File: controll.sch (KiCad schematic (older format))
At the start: 0 parts

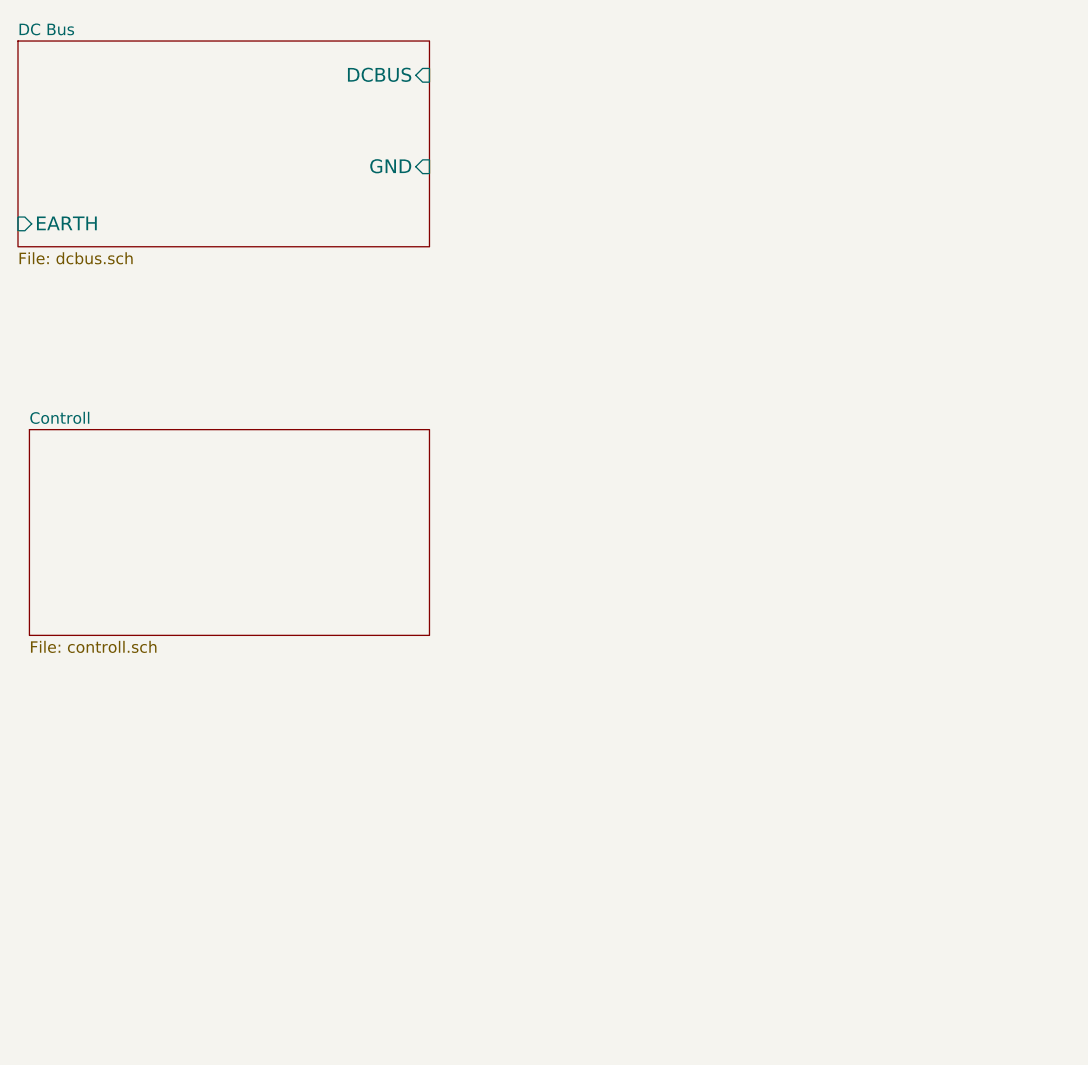
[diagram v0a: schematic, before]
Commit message: add placeholder for controll schematics
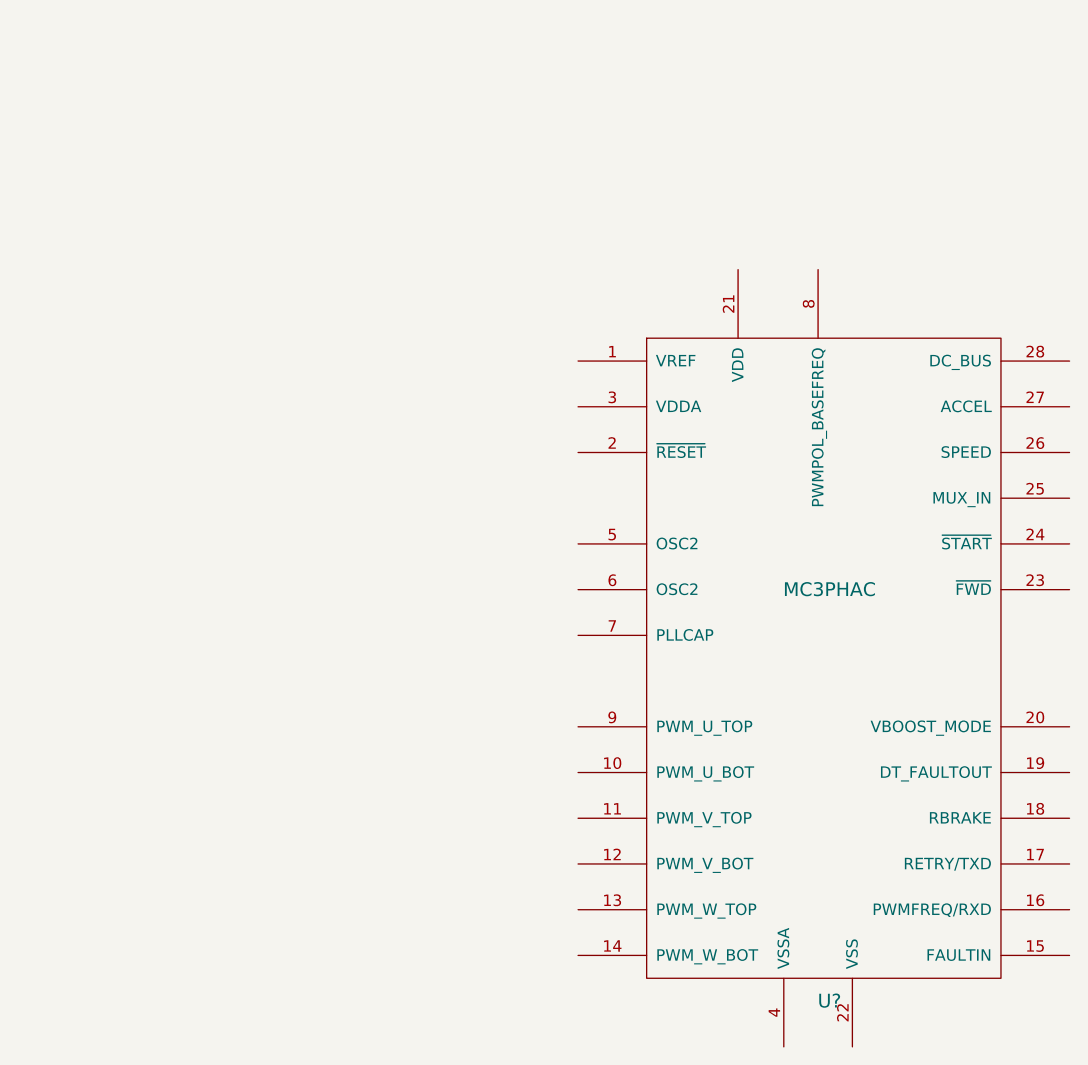
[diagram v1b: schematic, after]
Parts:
- added U?: MC3PHAC, symbol MC3PHAC
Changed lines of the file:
@@
 $Descr A4 11693 8268
 encoding utf-8
-Sheet 1 3
+Sheet 3 3
 Title ""
 Date ""
@@
 Comment4 ""
 $EndDescr
-$Sheet
-S 1450 1400 1800 900
-U 5377D90A
-F0 "DC Bus" 50
-F1 "dcbus.sch" 50
-F2 "DCBUS" I R 3250 1550 60
-F3 "GND" I R 3250 1950 60
-F4 "EARTH" I L 1450 2200 60
-$EndSheet
-$Sheet
-S 1500 3100 1750 900
-U 537BA57E
-F0 "Controll" 50
-F1 "controll.sch" 50
-$EndSheet
+$Comp
+L MC3PHAC U?
+U 1 1 537BA586
+P 4950 4000
+F 0 "U?" H 5000 2400 60  0000 C CNN
+F 1 "MC3PHAC" H 5000 4200 60  0000 C CNN
+F 2 "" H 5250 4450 60  0000 C CNN
+F 3 "" H 5250 4450 60  0000 C CNN
+	1    4950 4000
+	1    0    0    -1
+$EndComp
 $EndSCHEMATC

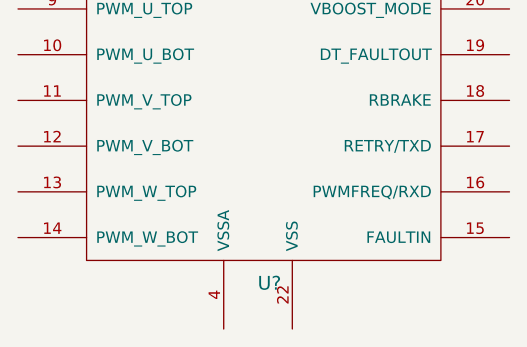
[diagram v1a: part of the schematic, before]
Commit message: add snubbing, mov for the main cap protection and a bleeder resistor for the main cap. add annotations finally
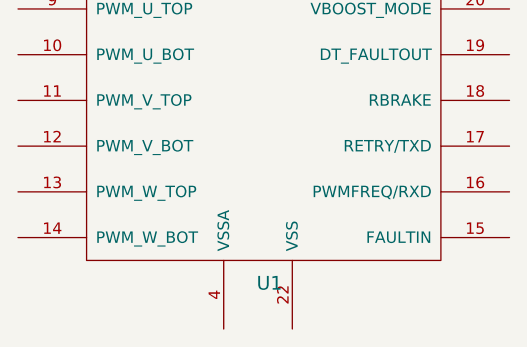
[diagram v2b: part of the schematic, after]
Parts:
- gave numbers to parts that had none: 1
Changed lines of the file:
@@
 $EndDescr
 $Comp
-L MC3PHAC U?
+L MC3PHAC U1
 U 1 1 537BA586
 P 4950 4000
-F 0 "U?" H 5000 2400 60  0000 C CNN
+F 0 "U1" H 5000 2400 60  0000 C CNN
 F 1 "MC3PHAC" H 5000 4200 60  0000 C CNN
 F 2 "" H 5250 4450 60  0000 C CNN

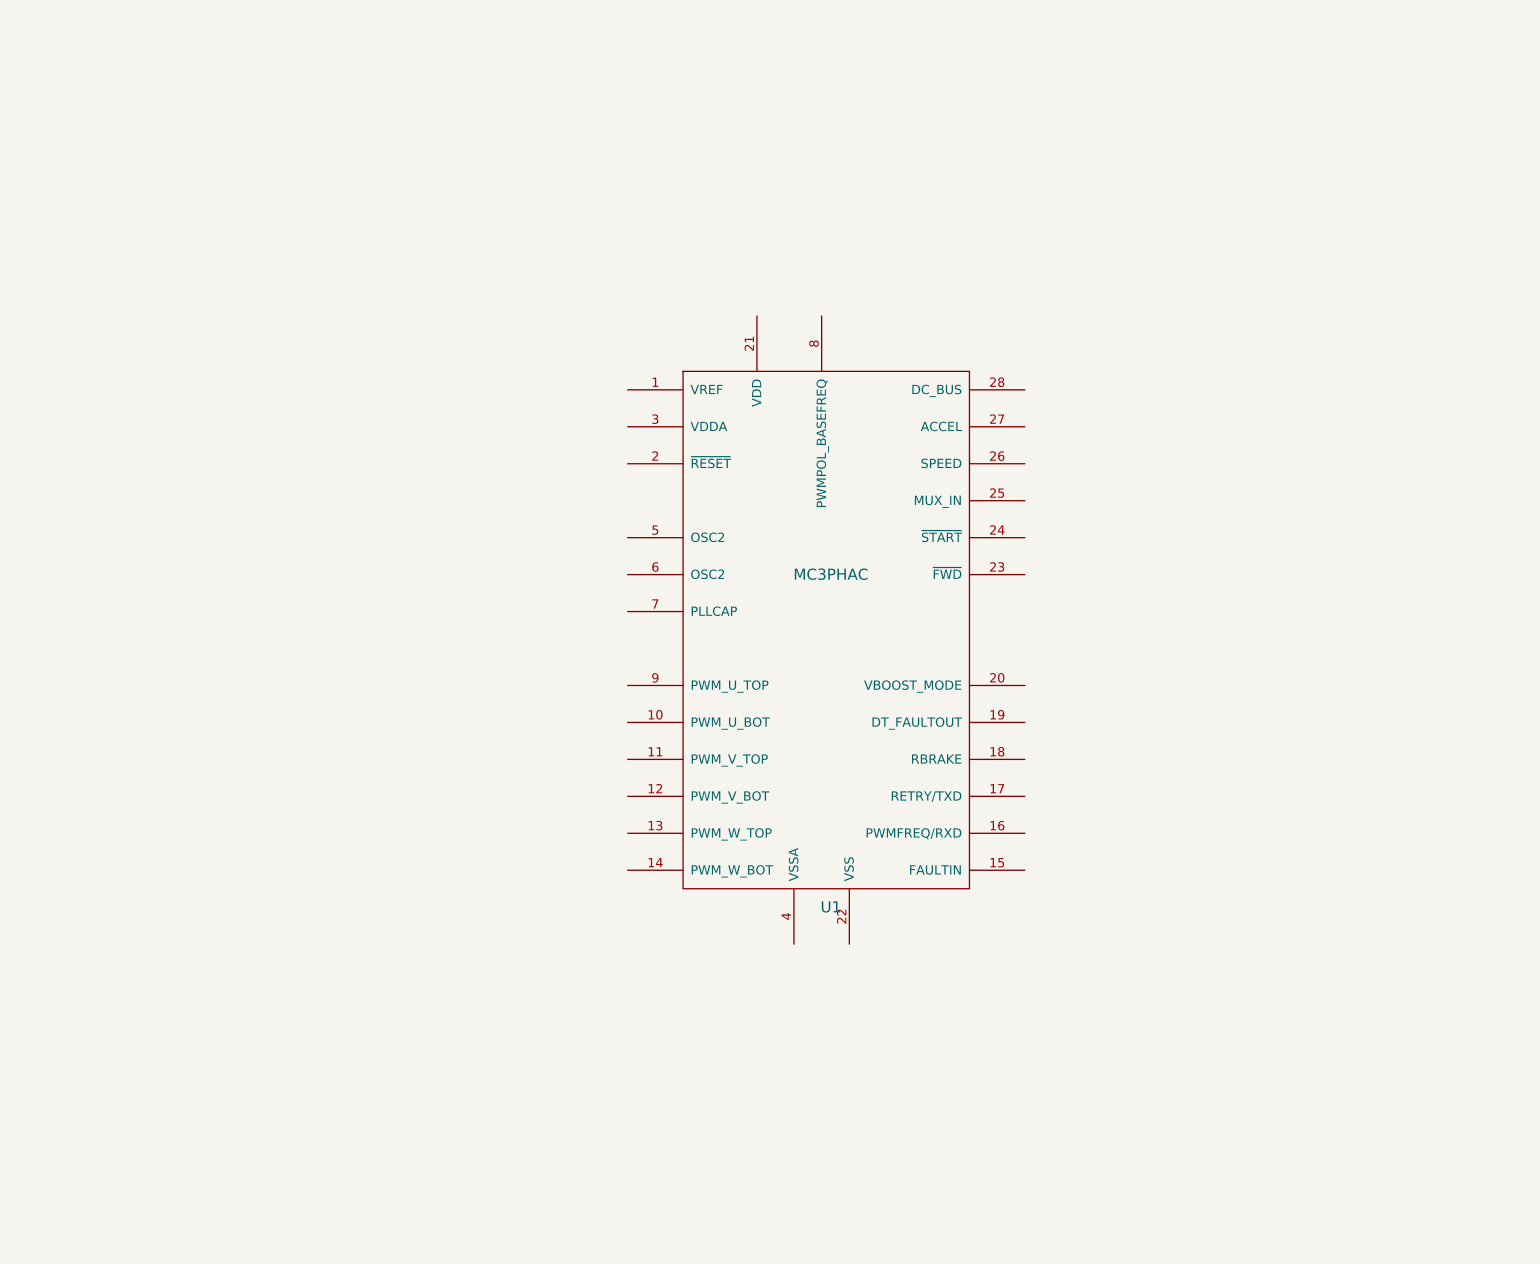
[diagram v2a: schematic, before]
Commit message: started populating contoll part
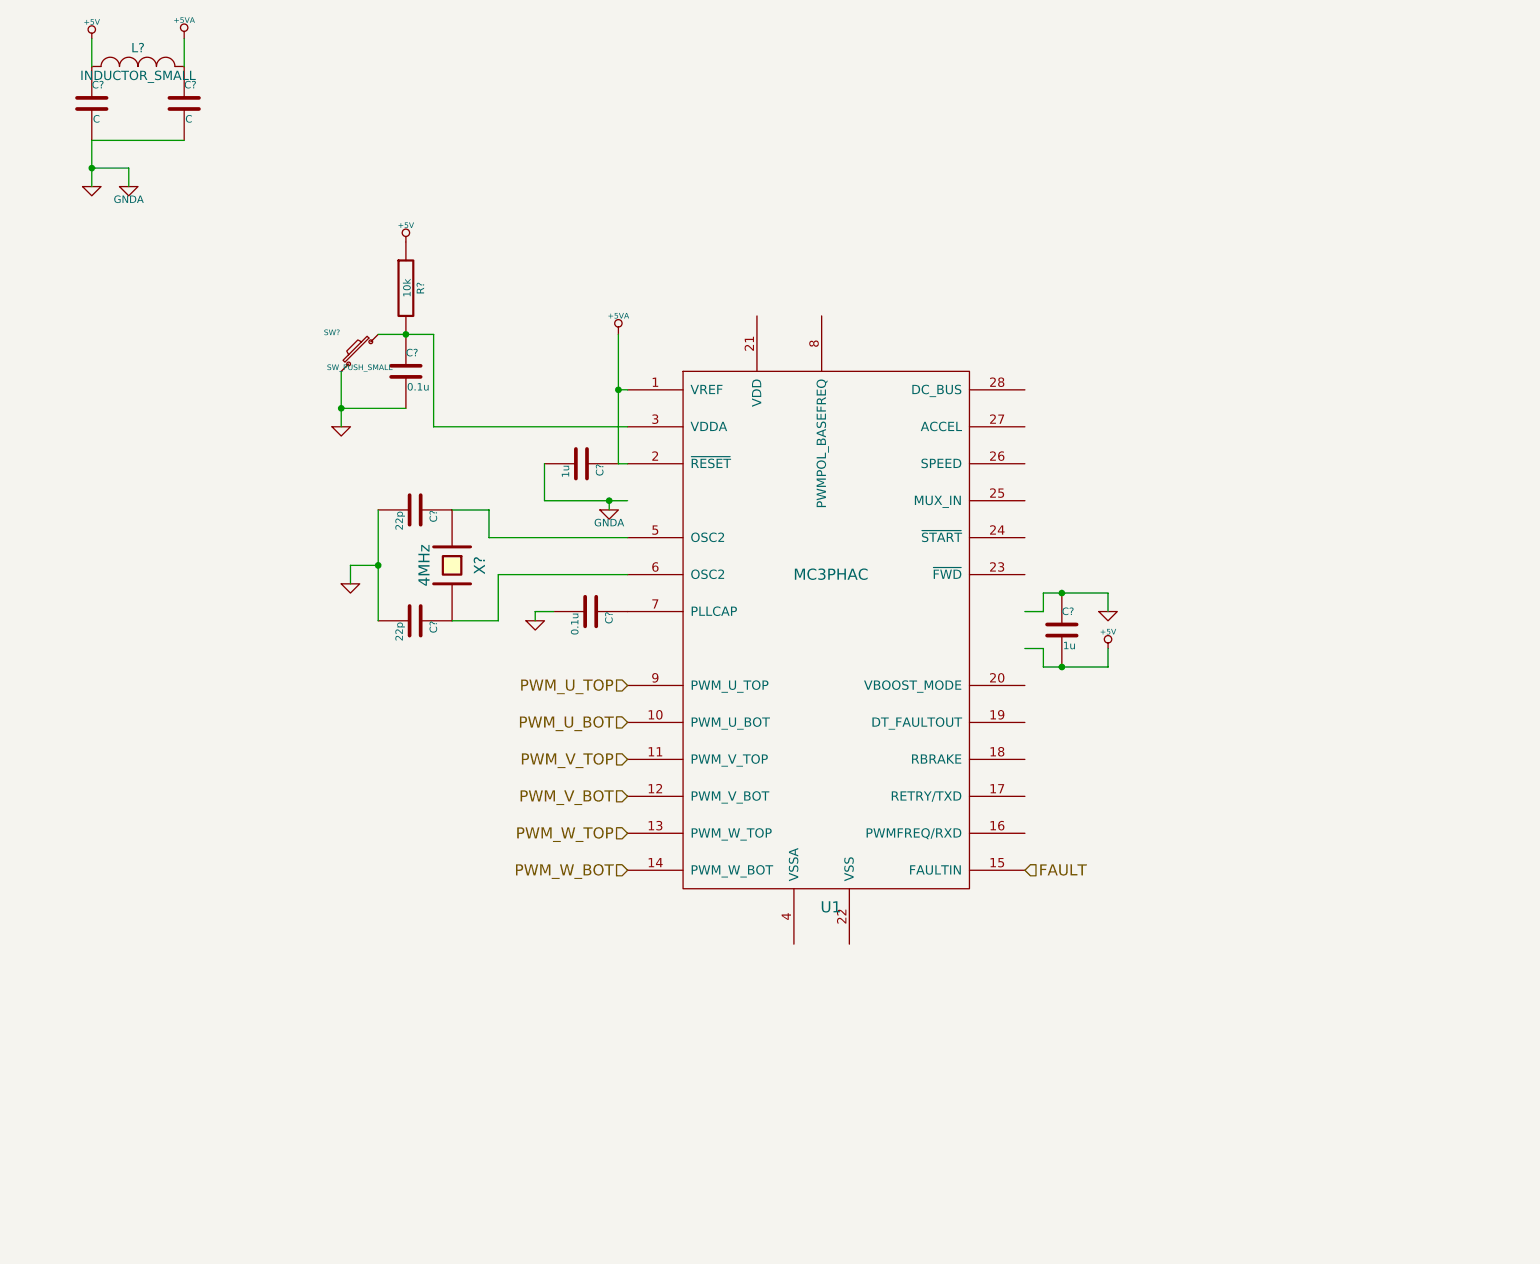
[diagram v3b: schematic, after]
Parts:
- added C? (x2): 22p, symbol C
- added C? (x2): 0.1u, symbol C
- added C? (x2): 1u, symbol C
- added C? (x2): C, symbol C
- added L?: INDUCTOR_SMALL, symbol INDUCTOR_SMALL
- added R?: 10k, symbol R
- added SW?: SW_PUSH_SMALL, symbol SW_PUSH_SMALL
- added X?: 4MHz, symbol CRYSTAL
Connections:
- net labels added: +5V, +5VA, FAULT, GND, GNDA, PWM_U_BOT, PWM_U_TOP, PWM_V_BOT, PWM_V_TOP, PWM_W_BOT, PWM_W_TOP
- wire segments 0 -> 36

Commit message: begin working on output power stage
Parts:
- removed SW?: SW_PUSH_SMALL, symbol SW_PUSH_SMALL
- added C14, C18: 100uF, symbol CP1
- added C15: 100nF, symbol C
- added C16: 10nF, symbol C
- added C17: 1nF, symbol C
- added JP1: 50Hz -, symbol JUMPER
- added JP2: 50Hz +, symbol JUMPER
- added JP3: 60Hz -, symbol JUMPER
- added JP4: 60Hz +, symbol JUMPER
- added P1: CONN_12, symbol CONN_12
- added P2, P3: CONN_6, symbol CONN_6
- added P4: CONN_4, symbol CONN_4
- added R10, R11, R12, R9: R, symbol R
- added R13, R14: 10k, symbol R
- added R6: 6.8k, symbol R
- added R7, R8: 4.7k, symbol R
- added SW1: SPST, symbol SPST
- C7: renamed from C?; value C -> 1uF
- gave numbers to parts that had none: 10
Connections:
- net labels added: ACCEL, DCBUSSENSE, RBRAKE, RXD, SPEED, TXD, ~FWD, ~START
- wire segments 36 -> 101
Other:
- moved on the sheet: C11, C13, C8, R5

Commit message: populating boards
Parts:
- added C?: 1n, symbol C
- added IC1: FOD8012, SOP-8, symbol FOD8012
- added R?: 100R, symbol R
- added R?: 4.7k, symbol R
- added SW4: PC/STANDALONE, symbol SWITCH_INV
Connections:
- net +5V: now also IC1.1, R?.1; no longer P4.4 (P4)
- net FAULT: now also C?.1, R?.1, R?.2; no longer U1.15 (FAULTIN)
- net GND: now also C?.2, IC1.4, SW4.3; no longer P4.2 (P2)
- net RXD: now also IC1.7; no longer R12.2, U1.16 (PWMFREQ/RXD)
- net TXD: now also IC1.6; no longer R11.2, U1.17 (RETRY/TXD)
- net at U1.20 (VBOOST_MODE): now also SW4.2; no longer R9.2
- new net: R?.2, U1.15 (FAULTIN)
- new net: IC1.2, R12.2, U1.16 (PWMFREQ/RXD)
- new net: IC1.3, R11.2, U1.17 (RETRY/TXD)
- new net: R9.2, SW4.1
- new net GND_UART: IC1.5, P4.2 (P2)
- new net V_UART: IC1.8, P4.4 (P4)
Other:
- moved on the sheet: R9

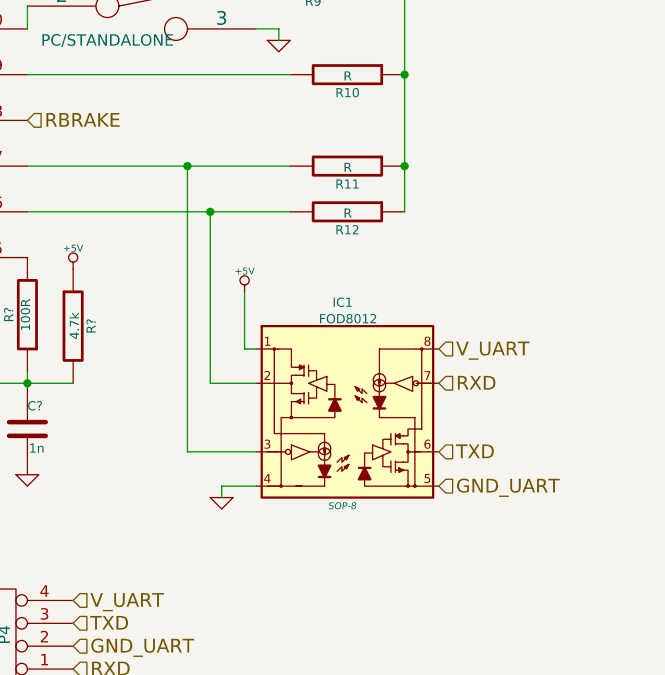
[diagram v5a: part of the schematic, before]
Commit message: fod8012 changed to cpc5001
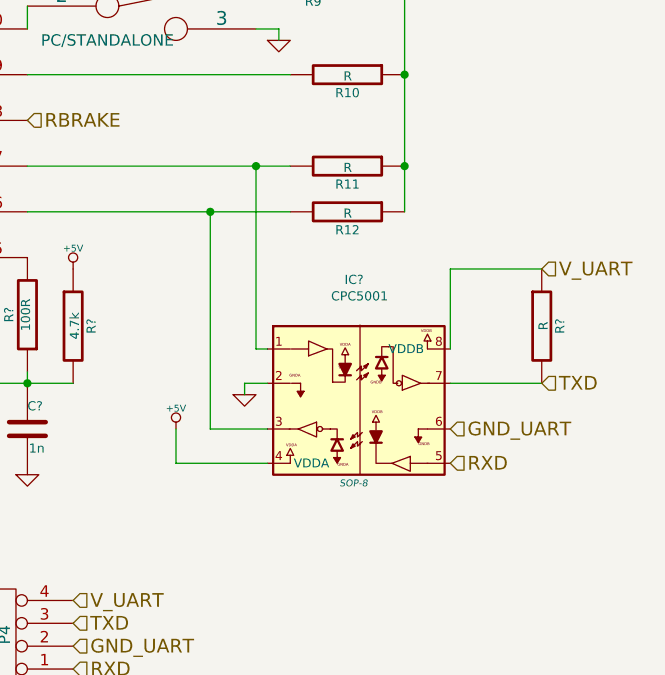
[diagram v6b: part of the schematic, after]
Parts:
- removed IC1: FOD8012, SOP-8, symbol FOD8012
- added IC?: CPC5001, SOP-8, symbol CPC5001
- added R?: R, symbol R
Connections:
- net +5V: now also IC?.4 (VDDA)
- net GND: now also IC?.2
- net GND_UART: now also IC?.6
- net RXD: now also IC?.5
- net TXD: now also IC?.7, R?.2
- net V_UART: now also IC?.8 (VDDB), R?.1
- net at R12.2, U1.16 (PWMFREQ/RXD): now also IC?.3
- net at R11.2, U1.17 (RETRY/TXD): now also IC?.1
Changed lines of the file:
@@
 	1    0    0    -1
 $EndComp
-Text HLabel 7850 6250 2    60   Input ~ 0
+Text HLabel 8300 5950 2    60   Input ~ 0
 TXD
-Text HLabel 7850 5950 2    60   Input ~ 0
+Text HLabel 7900 6300 2    60   Input ~ 0
 RXD
 $Comp
@@
 	6050 5200 7200 5200
 Wire Wire Line
-	6750 5000 6750 6250
-Connection ~ 6750 5000
-Wire Wire Line
 	1950 6050 2750 6050
 Wire Wire Line
@@
 Wire Wire Line
 	7150 4400 7050 4400
-$Comp
-L FOD8012 IC1
-U 1 1 538A4C86
-P 7450 6150
-F 0 "IC1" H 7429 6703 40  0000 C CNN
-F 1 "FOD8012" H 7453 6631 40  0000 C CNN
-F 2 "SOP-8" H 7427 5813 30  0000 C CIN
-F 3 "" H 7430 5995 60  0000 C CNN
-	1    7450 6150
-	1    0    0    -1
-$EndComp
-Wire Wire Line
-	6750 6250 7050 6250
-Wire Wire Line
-	7050 5950 6850 5950
-Wire Wire Line
-	6850 5950 6850 5200
 Connection ~ 6850 5200
 $Comp
 L +5V #PWR27
 U 1 1 538A5075
-P 7000 5550
-F 0 "#PWR27" H 7000 5640 20  0001 C CNN
-F 1 "+5V" H 7000 5640 30  0000 C CNN
-F 2 "" H 7000 5550 60  0000 C CNN
-F 3 "" H 7000 5550 60  0000 C CNN
-	1    7000 5550
+P 6700 6150
+F 0 "#PWR27" H 6700 6240 20  0001 C CNN
+F 1 "+5V" H 6700 6240 30  0000 C CNN
+F 2 "" H 6700 6150 60  0000 C CNN
+F 3 "" H 6700 6150 60  0000 C CNN
+	1    6700 6150
 	1    0    0    -1
 $EndComp
@@
 L GND #PWR26
 U 1 1 538A51B1
-P 6900 6450
-F 0 "#PWR26" H 6900 6450 30  0001 C CNN
-F 1 "GND" H 6900 6380 30  0001 C CNN
-F 2 "" H 6900 6450 60  0000 C CNN
-F 3 "" H 6900 6450 60  0000 C CNN
-	1    6900 6450
-	1    0    0    -1
-$EndComp
-Wire Wire Line
-	6900 6450 6900 6400
-Wire Wire Line
-	6900 6400 7050 6400
-Wire Wire Line
-	7000 5550 7000 5800
-Wire Wire Line
-	7000 5800 7050 5800
-Text HLabel 7850 5800 2    60   Input ~ 0
+P 7000 6000
+F 0 "#PWR26" H 7000 6000 30  0001 C CNN
+F 1 "GND" H 7000 5930 30  0001 C CNN
+F 2 "" H 7000 6000 60  0000 C CNN
+F 3 "" H 7000 6000 60  0000 C CNN
+	1    7000 6000
+	1    0    0    -1
+$EndComp
+Text HLabel 8300 5450 2    60   Input ~ 0
 V_UART
-Text HLabel 7850 6400 2    60   Input ~ 0
+Text HLabel 7900 6150 2    60   Input ~ 0
 GND_UART
 Text HLabel 6250 7200 2    60   Input ~ 0
@@
 	5900 5950 6250 5950
 Connection ~ 6050 5950
+$Comp
+L CPC5001 IC?
+U 1 1 538A060B
+P 7500 6050
+F 0 "IC?" H 7479 6603 40  0000 C CNN
+F 1 "CPC5001" H 7503 6531 40  0000 C CNN
+F 2 "SOP-8" H 7477 5713 30  0000 C CIN
+F 3 "" H 7490 5905 60  0000 C CNN
+	1    7500 6050
+	1    0    0    -1
+$EndComp
+Wire Wire Line
+	7100 6150 6850 6150
+Wire Wire Line
+	6850 6150 6850 5200
+Wire Wire Line
+	7100 5800 7050 5800
+Wire Wire Line
+	7050 5800 7050 5000
+Connection ~ 7050 5000
+Wire Wire Line
+	6700 6150 6700 6300
+Wire Wire Line
+	6700 6300 7100 6300
+Wire Wire Line
+	7000 6000 7000 5950
+Wire Wire Line
+	7000 5950 7100 5950
+$Comp
+L R R?
+U 1 1 538A1306
+P 8300 5700
+F 0 "R?" V 8380 5700 40  0000 C CNN
+F 1 "R" V 8307 5701 40  0000 C CNN
+F 2 "" V 8230 5700 30  0000 C CNN
+F 3 "" H 8300 5700 30  0000 C CNN
+	1    8300 5700
+	1    0    0    -1
+$EndComp
+Wire Wire Line
+	8300 5950 7900 5950
+Wire Wire Line
+	7900 5800 7900 5450
+Wire Wire Line
+	7900 5450 8300 5450
 $EndSCHEMATC
